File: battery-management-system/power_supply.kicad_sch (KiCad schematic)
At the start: 23 parts, among them U1 L6982C33DR, U2 L6982C33DR

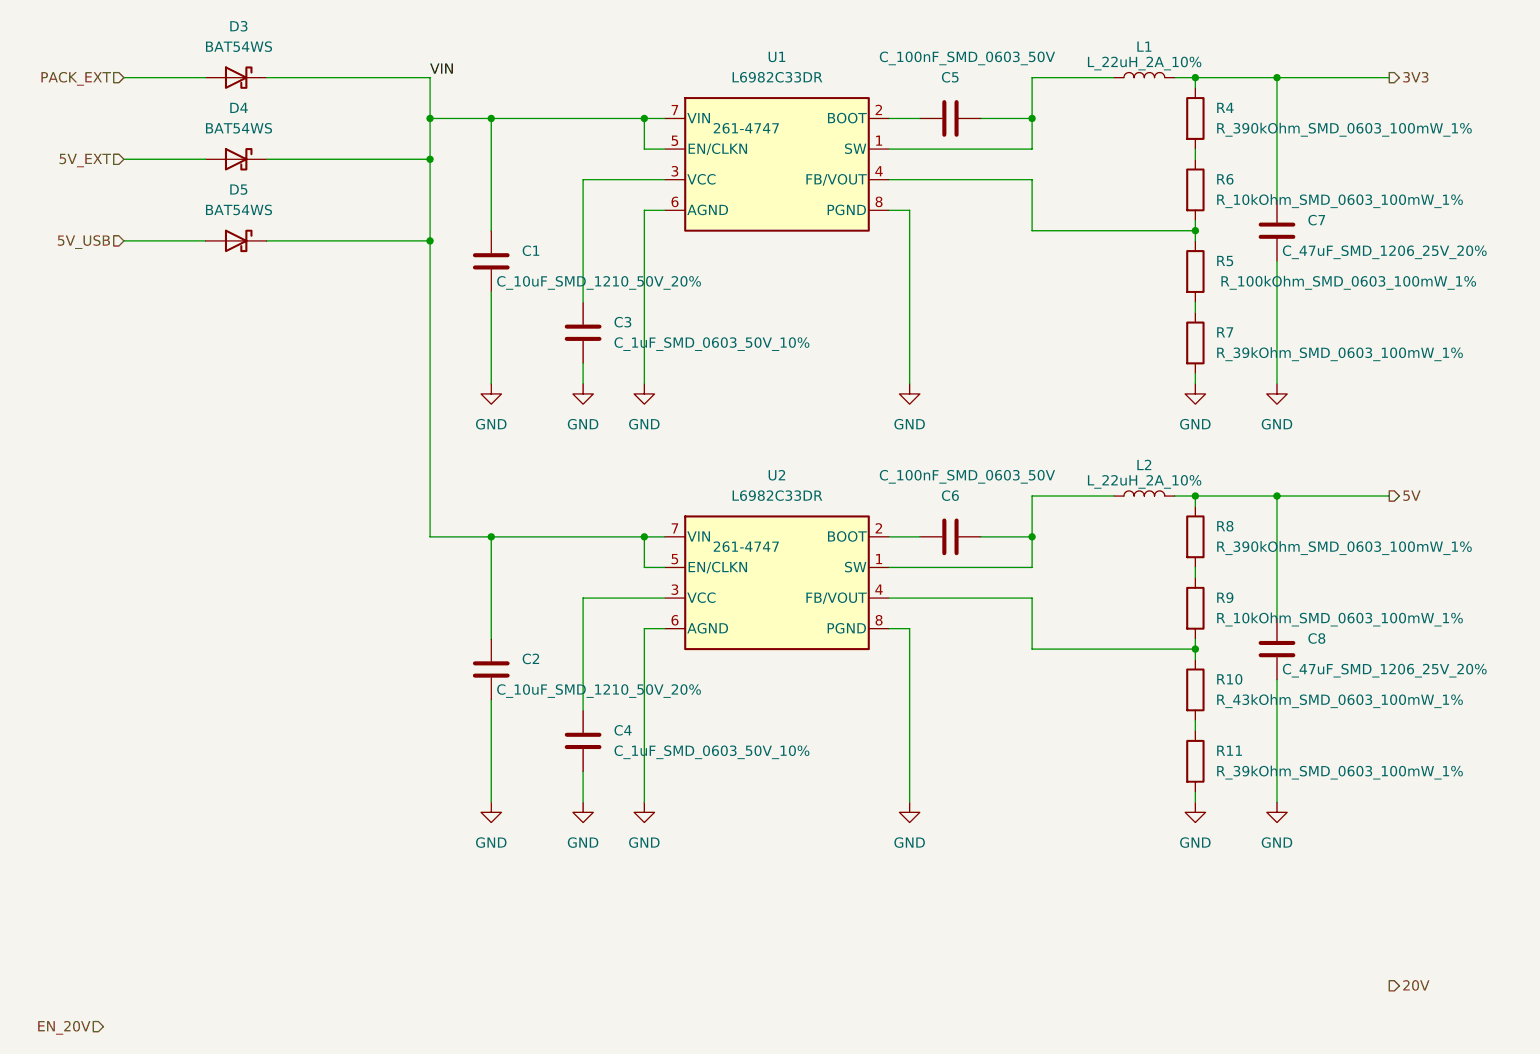
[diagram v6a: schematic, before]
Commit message: use M6 connectors, update symbols
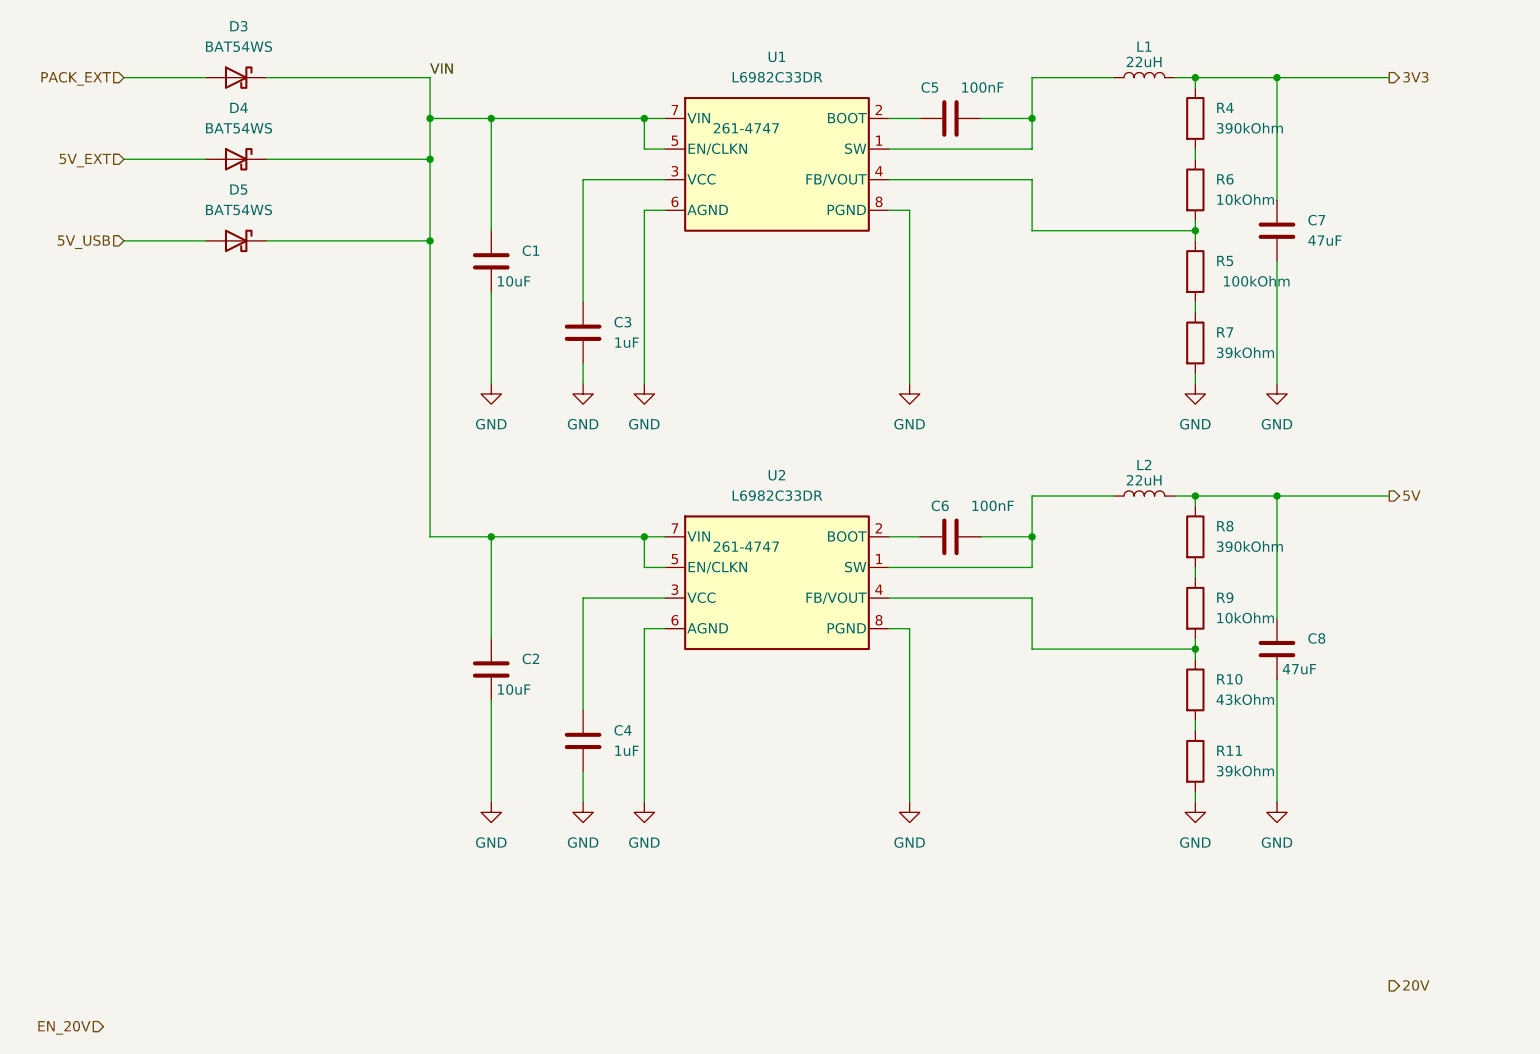
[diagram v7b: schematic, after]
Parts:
- C1, C2: value C_10uF_SMD_1210_50V_20% -> 10uF
- C3, C4: value C_1uF_SMD_0603_50V_10% -> 1uF
- C5, C6: value C_100nF_SMD_0603_50V -> 100nF
- C7, C8: value C_47uF_SMD_1206_25V_20% -> 47uF
- L1, L2: value L_22uH_2A_10% -> 22uH
- R10: value R_43kOhm_SMD_0603_100mW_1% -> 43kOhm
- R11, R7: value R_39kOhm_SMD_0603_100mW_1% -> 39kOhm
- R4, R8: value R_390kOhm_SMD_0603_100mW_1% -> 390kOhm
- R5: value R_100kOhm_SMD_0603_100mW_1% -> 100kOhm
- R6, R9: value R_10kOhm_SMD_0603_100mW_1% -> 10kOhm
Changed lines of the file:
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@@
       (effects (font (size 1.27 1.27)) (justify left))
     )
-    (property "Value" "R_10kOhm_SMD_0603_100mW_1%" (id 1) (at 165.1 87.63 0)
+    (property "Value" "10kOhm" (id 1) (at 165.1 87.63 0)
       (effects (font (size 1.27 1.27)) (justify left))
     )
@@
       (effects (font (size 1.27 1.27)) (justify left))
     )
-    (property "Value" "R_390kOhm_SMD_0603_100mW_1%" (id 1) (at 165.1 26.6699 0)
+    (property "Value" "390kOhm" (id 1) (at 165.1 26.6699 0)
       (effects (font (size 1.27 1.27)) (justify left))
     )
@@
       (effects (font (size 1.27 1.27)) (justify left))
     )
-    (property "Value" "R_390kOhm_SMD_0603_100mW_1%" (id 1) (at 165.1 78.7399 0)
+    (property "Value" "390kOhm" (id 1) (at 165.1 78.7399 0)
       (effects (font (size 1.27 1.27)) (justify left))
     )
@@
       (effects (font (size 1.27 1.27)) (justify left))
     )
-    (property "Value" "R_39kOhm_SMD_0603_100mW_1%" (id 1) (at 165.1 106.6799 0)
+    (property "Value" "39kOhm" (id 1) (at 165.1 106.6799 0)
       (effects (font (size 1.27 1.27)) (justify left))
     )
@@
   (symbol (lib_id "benediktibk:C_100nF_SMD_0603_50V") (at 132.08 77.47 270) (unit 1)
     (in_bom yes) (on_board yes)
-    (property "Reference" "C6" (id 0) (at 132.08 72.39 90))
-    (property "Value" "C_100nF_SMD_0603_50V" (id 1) (at 123.19 69.85 90)
+    (property "Reference" "C6" (id 0) (at 130.81 73.66 90))
+    (property "Value" "100nF" (id 1) (at 134.62 73.66 90)
       (effects (font (size 1.27 1.27)) (justify left))
     )
@@
       (effects (font (size 1.27 1.27)) (justify left))
     )
-    (property "Value" "C_47uF_SMD_1206_25V_20%" (id 1) (at 173.355 41.91 0)
+    (property "Value" "47uF" (id 1) (at 176.53 40.6399 0)
       (effects (font (size 1.27 1.27)) (justify left))
     )
@@
       (effects (font (size 1.27 1.27)) (justify left))
     )
-    (property "Value" "C_10uF_SMD_1210_50V_20%" (id 1) (at 75.565 96.52 0)
+    (property "Value" "10uF" (id 1) (at 75.565 96.52 0)
       (effects (font (size 1.27 1.27)) (justify left))
     )
@@
       (effects (font (size 1.27 1.27)) (justify left))
     )
-    (property "Value" "C_1uF_SMD_0603_50V_10%" (id 1) (at 90.17 104.1399 0)
+    (property "Value" "1uF" (id 1) (at 90.17 104.1399 0)
       (effects (font (size 1.27 1.27)) (justify left))
     )
@@
       (effects (font (size 1.27 1.27)) (justify left))
     )
-    (property "Value" "C_10uF_SMD_1210_50V_20%" (id 1) (at 75.565 45.72 0)
+    (property "Value" "10uF" (id 1) (at 75.565 45.72 0)
       (effects (font (size 1.27 1.27)) (justify left))
     )
@@
     (in_bom yes) (on_board yes)
     (property "Reference" "L1" (id 0) (at 156.21 16.51 90))
-    (property "Value" "L_22uH_2A_10%" (id 1) (at 156.21 18.415 90))
+    (property "Value" "22uH" (id 1) (at 156.21 18.415 90))
     (property "Footprint" "benediktibk:L_Radial_D9.5mm_P5.00mm_Fastron_07HVP" (id 2) (at 156.21 20.32 0)
       (effects (font (size 1.27 1.27)) hide)
@@
       (effects (font (size 1.27 1.27)) (justify left))
     )
-    (property "Value" "R_100kOhm_SMD_0603_100mW_1%" (id 1) (at 181.61 45.72 0))
+    (property "Value" "100kOhm" (id 1) (at 170.18 45.72 0))
     (property "Footprint" "benediktibk:R_0603_1608Metric_Pad0.98x0.95mm_HandSolder" (id 2) (at 152.4 43.942 90)
       (effects (font (size 1.27 1.27)) hide)
@@
       (effects (font (size 1.27 1.27)) (justify left))
     )
-    (property "Value" "R_39kOhm_SMD_0603_100mW_1%" (id 1) (at 165.1 54.6099 0)
+    (property "Value" "39kOhm" (id 1) (at 165.1 54.6099 0)
       (effects (font (size 1.27 1.27)) (justify left))
     )
@@
       (effects (font (size 1.27 1.27)) (justify left))
     )
-    (property "Value" "C_1uF_SMD_0603_50V_10%" (id 1) (at 90.17 53.3399 0)
+    (property "Value" "1uF" (id 1) (at 90.17 53.3399 0)
       (effects (font (size 1.27 1.27)) (justify left))
     )
@@
       (effects (font (size 1.27 1.27)) (justify left))
     )
-    (property "Value" "C_47uF_SMD_1206_25V_20%" (id 1) (at 173.355 93.98 0)
+    (property "Value" "47uF" (id 1) (at 173.355 93.98 0)
       (effects (font (size 1.27 1.27)) (justify left))
     )
@@
     (in_bom yes) (on_board yes)
     (property "Reference" "L2" (id 0) (at 156.21 68.58 90))
-    (property "Value" "L_22uH_2A_10%" (id 1) (at 156.21 70.485 90))
+    (property "Value" "22uH" (id 1) (at 156.21 70.485 90))
     (property "Footprint" "benediktibk:L_Radial_D9.5mm_P5.00mm_Fastron_07HVP" (id 2) (at 156.21 72.39 0)
       (effects (font (size 1.27 1.27)) hide)
@@
   (symbol (lib_id "benediktibk:C_100nF_SMD_0603_50V") (at 132.08 25.4 270) (unit 1)
     (in_bom yes) (on_board yes)
-    (property "Reference" "C5" (id 0) (at 132.08 20.32 90))
-    (property "Value" "C_100nF_SMD_0603_50V" (id 1) (at 123.19 17.78 90)
+    (property "Reference" "C5" (id 0) (at 129.54 21.59 90))
+    (property "Value" "100nF" (id 1) (at 133.35 21.59 90)
       (effects (font (size 1.27 1.27)) (justify left))
     )
@@
       (effects (font (size 1.27 1.27)) (justify left))
     )
-    (property "Value" "R_43kOhm_SMD_0603_100mW_1%" (id 1) (at 165.1 97.7899 0)
+    (property "Value" "43kOhm" (id 1) (at 165.1 97.7899 0)
       (effects (font (size 1.27 1.27)) (justify left))
     )
@@
       (effects (font (size 1.27 1.27)) (justify left))
     )
-    (property "Value" "R_10kOhm_SMD_0603_100mW_1%" (id 1) (at 165.1 35.56 0)
-      (effects (font (size 1.27 1.27)) (justify left))
-    )
+    (property "Value" "10kOhm" (id 1) (at 165.1 35.56 0)
+      (effects (font (size 1.27 1.27)) (justify left))
+    )

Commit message: add components
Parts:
- added J14: SUPPLY, benediktibk:PinHeader_1x03_P2.54mm_Vertical, symbol benediktibk:Conn_01x03
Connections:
- net GND: now also J14.3 (Pin_3)
- net VIN: now also J14.2 (Pin_2); no longer D3.1 (K), D4.1 (K), D5.1 (K)
- new net: D3.1 (K), D4.1 (K), D5.1 (K), J14.1 (Pin_1)
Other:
- moved on the sheet: D3, D4, D5
